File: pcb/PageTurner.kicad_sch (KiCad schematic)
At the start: 22 parts, among them J1 AudioJack2, J2 AudioJack2, J3 USB_C_Receptacle, J5 TC2030_SWD, SW1 RST, SW2 BOOT, U1 STM32F042F6Px, U2 TPS7A0533PDBV

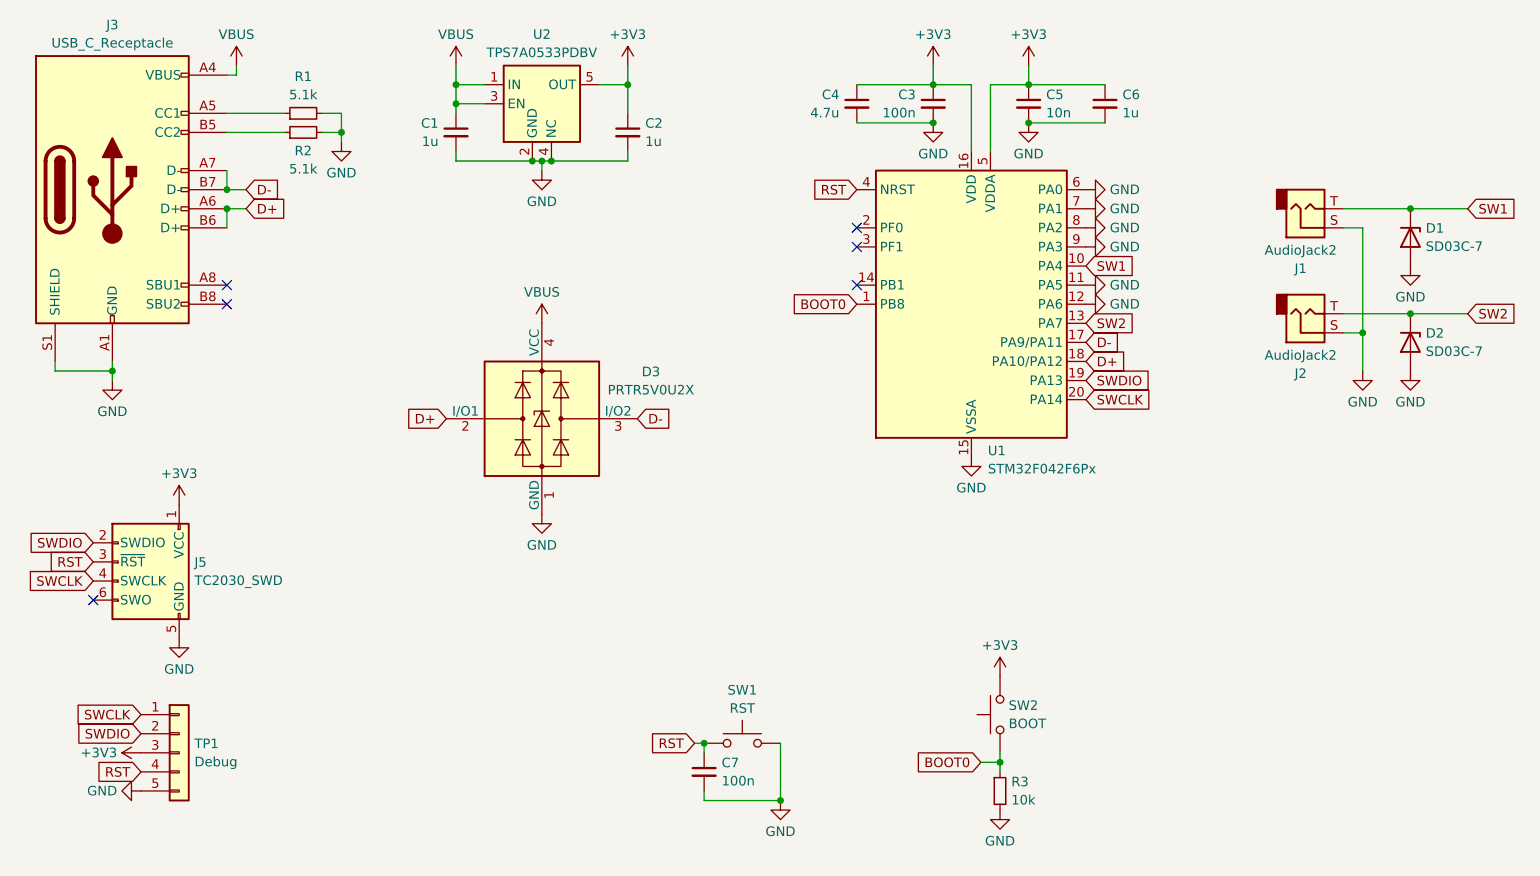
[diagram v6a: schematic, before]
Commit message: Disconnect GPIOs from GND
GPIOs are supposed to power up in floating input mode, so I tied some of
them to GND for easier routing. For some reason the input voltage sagged
to ~0.6 V until I disconnected these pins from the PCB though. I'm not
sure if this was the cause or I just messed up soldering something, but
disconnecting these just to be safe.
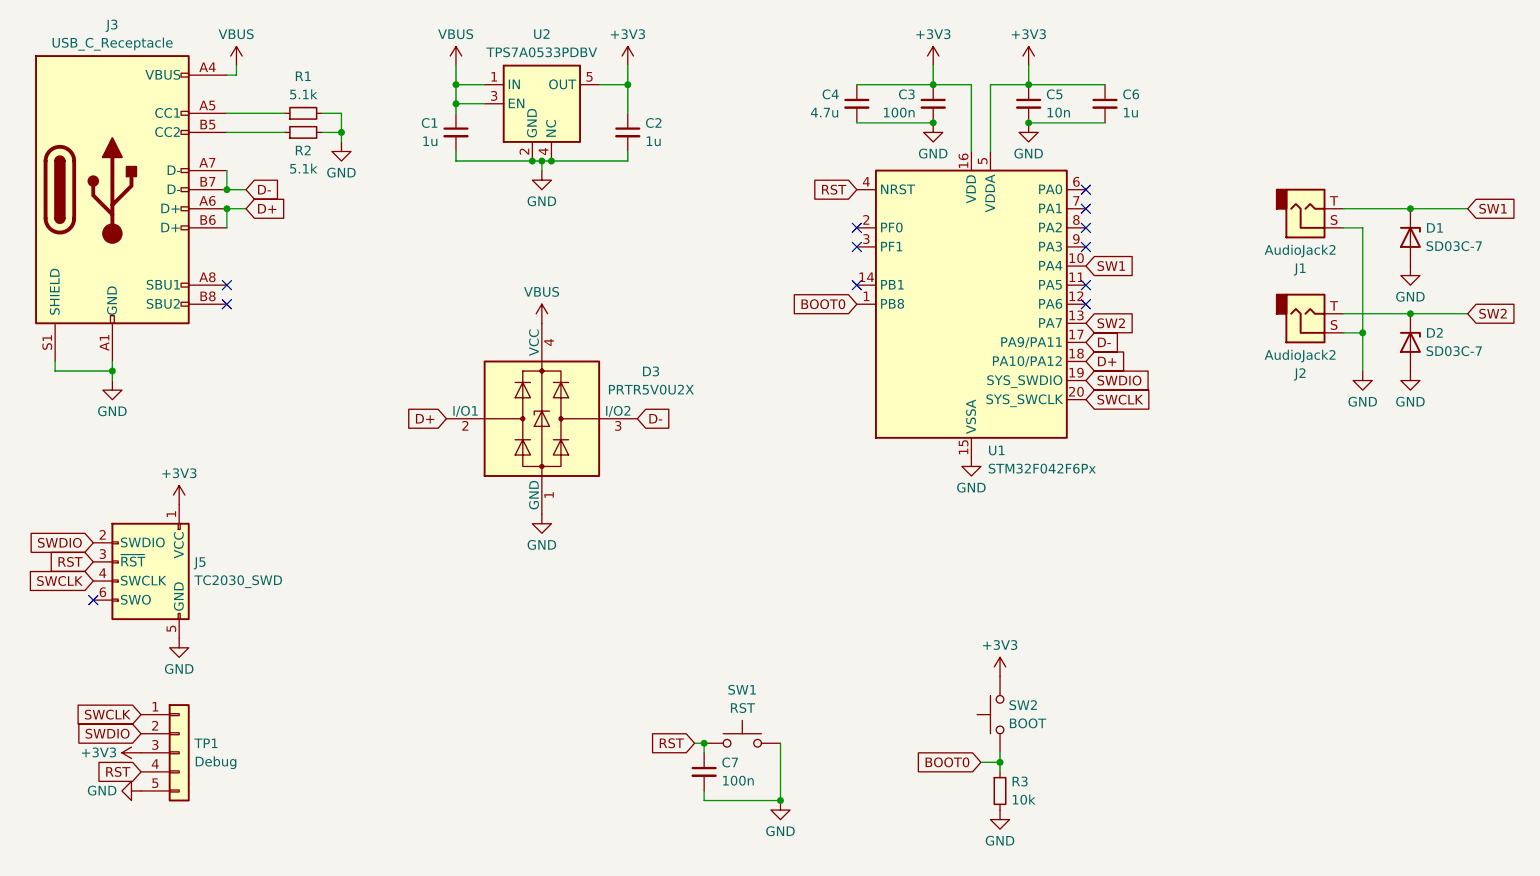
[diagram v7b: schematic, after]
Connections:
- net GND: no longer U1.11 (PA5), U1.12 (PA6), U1.6 (PA0), U1.7 (PA1), U1.8 (PA2), U1.9 (PA3)
- no-connect marks 6 -> 12
